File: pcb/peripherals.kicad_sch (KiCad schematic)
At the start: 35 parts, among them J2 Conn_01x24_MountingPin, J3 Conn_02x04_Odd_Even, J4 Conn_02x05_Odd_Even, SW1 SS-3235S-L1, U4 TLV74328PDBVR, U5 NRF24L01_Breakout, U6 TLV74315PDBVR, U7 BMI270, U8 HYCW110-TF10-180B, X1 OT322524MJBA4SL

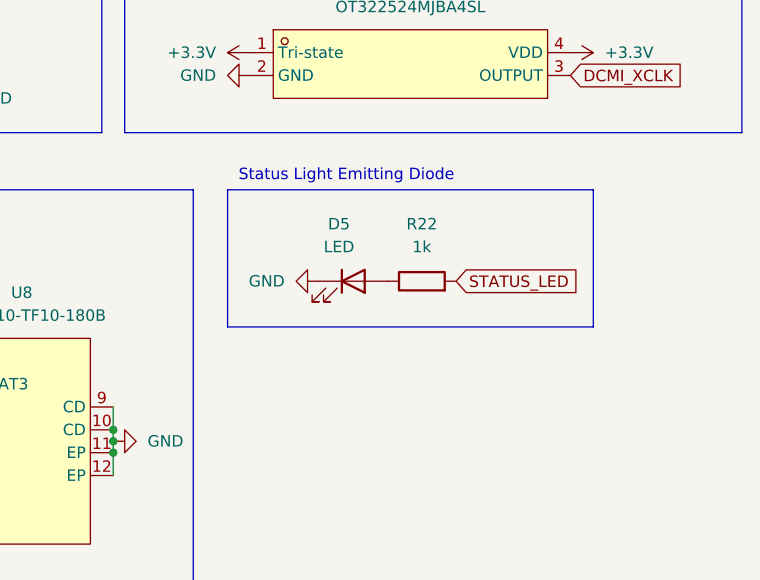
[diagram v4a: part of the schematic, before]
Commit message: [pcb] small fixes and improvements
- add two status LEDs
- move silkscreen labels for better visibility
- add more silkcreen logos/credits
- fix nrf footprint, add rf keepout zone
- add mounting holes
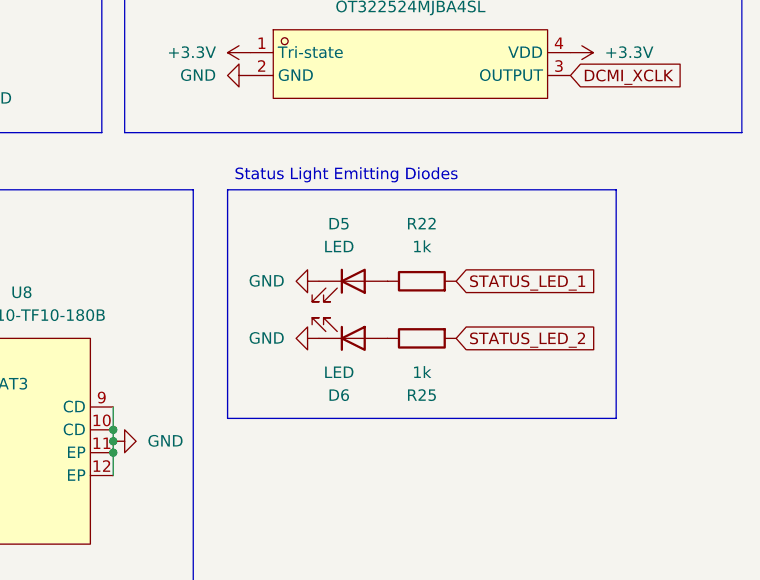
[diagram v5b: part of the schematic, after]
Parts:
- added D6: LED, LED_SMD:LED_0805_2012Metric, symbol Device:LED
- added R25: 1k, Resistor_SMD:R_0805_2012Metric, symbol Device:R
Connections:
- net GND: now also D6.1 (K)
- net STATUS_LED renamed STATUS_LED_1
- new net: D6.2 (A), R25.1
- new net STATUS_LED_2: R25.2
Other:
- note added: "Status Light Emitting Diodes"
- note removed: "Status Light Emitting Diode"
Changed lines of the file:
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@@
 	(rectangle
 		(start 165.1 100.33)
-		(end 205.74 115.57)
+		(end 208.28 125.73)
 		(stroke
 			(width 0)
@@
 		)
 	)
-	(text "Status Light Emitting Diode"
+	(text "Status Light Emitting Diodes"
 		(exclude_from_sim no)
 		(at 178.308 98.806 0)
@@
 		)
 	)
-	(global_label "STATUS_LED"
+	(global_label "STATUS_LED_1"
 		(shape input)
 		(at 190.5 110.49 0)
@@
 		)
 		(property "Intersheetrefs" "${INTERSHEET_REFS}"
-			(at 204.6732 110.49 0)
+			(at 206.8503 110.49 0)
 			(effects
 				(font
@@
 		)
 	)
+	(global_label "STATUS_LED_2"
+		(shape input)
+		(at 190.5 116.84 0)
+		(fields_autoplaced yes)
+		(effects
+			(font
+				(size 1.27 1.27)
+			)
+			(justify left)
+		)
+		(property "Intersheetrefs" "${INTERSHEET_REFS}"
+			(at 206.8503 116.84 0)
+			(effects
+				(font
+					(size 1.27 1.27)
+				)
+				(justify left)
+				(hide yes)
+			)
+		)
+	)
 	(global_label "DCMI_PWDN"
 		(shape input)
@@
 	)
 	(symbol
+		(lib_id "Device:R")
+		(at 186.69 116.84 90)
+		(mirror x)
+		(unit 1)
+		(exclude_from_sim no)
+		(in_bom yes)
+		(on_board yes)
+		(dnp no)
+		(fields_autoplaced yes)
+		(property "Reference" "R25"
+			(at 186.69 123.19 90)
+			(effects
+				(font
+					(size 1.27 1.27)
+				)
+			)
+		)
+		(property "Value" "1k"
+			(at 186.69 120.65 90)
+			(effects
+				(font
+					(size 1.27 1.27)
+				)
+			)
+		)
+		(property "Footprint" "Resistor_SMD:R_0805_2012Metric"
+			(at 186.69 115.062 90)
+			(effects
+				(font
+					(size 1.27 1.27)
+				)
+				(hide yes)
+			)
+		)
+		(property "Datasheet" "~"
+			(at 186.69 116.84 0)
+			(effects
+				(font
+					(size 1.27 1.27)
+				)
+				(hide yes)
+			)
+		)
+		(property "Description" "Resistor"
+			(at 186.69 116.84 0)
+			(effects
+				(font
+					(size 1.27 1.27)
+				)
+				(hide yes)
+			)
+		)
+		(pin "1"
+		)
+		(pin "2"
+		)
+		(instances
+			(project "astra"
+				(path "/c0be3de2-9de4-4447-aa6f-537ea5f31aac/5121fc52-65c9-43af-86a0-4c1ef24f194e"
+					(reference "R25")
+					(unit 1)
+				)
+			)
+		)
+	)
+	(symbol
 		(lib_id "power:+3.3V")
 		(at 97.79 52.07 270)
@@
 	(symbol
 		(lib_id "power:GND")
+		(at 175.26 116.84 270)
+		(mirror x)
+		(unit 1)
+		(exclude_from_sim no)
+		(in_bom yes)
+		(on_board yes)
+		(dnp no)
+		(fields_autoplaced yes)
+		(property "Reference" "#PWR083"
+			(at 168.91 116.84 0)
+			(effects
+				(font
+					(size 1.27 1.27)
+				)
+				(hide yes)
+			)
+		)
+		(property "Value" "GND"
+			(at 171.45 116.8401 90)
+			(effects
+				(font
+					(size 1.27 1.27)
+				)
+				(justify right)
+			)
+		)
+		(property "Footprint" ""
+			(at 175.26 116.84 0)
+			(effects
+				(font
+					(size 1.27 1.27)
+				)
+				(hide yes)
+			)
+		)
+		(property "Datasheet" ""
+			(at 175.26 116.84 0)
+			(effects
+				(font
+					(size 1.27 1.27)
+				)
+				(hide yes)
+			)
+		)
+		(property "Description" "Power symbol creates a global label with name \"GND\" , ground"
+			(at 175.26 116.84 0)
+			(effects
+				(font
+					(size 1.27 1.27)
+				)
+				(hide yes)
+			)
+		)
+		(pin "1"
+		)
+		(instances
+			(project "astra"
+				(path "/c0be3de2-9de4-4447-aa6f-537ea5f31aac/5121fc52-65c9-43af-86a0-4c1ef24f194e"
+					(reference "#PWR083")
+					(unit 1)
+				)
+			)
+		)
+	)
+	(symbol
+		(lib_id "power:GND")
 		(at 193.04 36.83 0)
 		(unit 1)
@@
 					(unit 1)
 				)
+			)
+		)
+	)
+	(symbol
+		(lib_id "Device:LED")
+		(at 179.07 116.84 0)
+		(mirror x)
+		(unit 1)
+		(exclude_from_sim no)
+		(in_bom yes)
+		(on_board yes)
+		(dnp no)
+		(fields_autoplaced yes)
+		(property "Reference" "D6"
+			(at 177.4825 123.19 0)
+			(effects
+				(font
+					(size 1.27 1.27)
+				)
+			)
+		)
+		(property "Value" "LED"
+			(at 177.4825 120.65 0)
+			(effects
+				(font
+					(size 1.27 1.27)
+				)
+			)
+		)
+		(property "Footprint" "LED_SMD:LED_0805_2012Metric"
+			(at 179.07 116.84 0)
+			(effects
+				(font
+					(size 1.27 1.27)
+				)
+				(hide yes)
+			)
+		)
+		(property "Datasheet" "~"
+			(at 179.07 116.84 0)
+			(effects
+				(font
+					(size 1.27 1.27)
+				)
+				(hide yes)
+			)
+		)
+		(property "Description" "Light emitting diode"
+			(at 179.07 116.84 0)
+			(effects
+				(font
+					(size 1.27 1.27)
+				)
+				(hide yes)
+			)
+		)
+		(property "Sim.Pins" "1=K 2=A"
+			(at 179.07 116.84 0)
+			(effects
+				(font
+					(size 1.27 1.27)
+				)
+				(hide yes)
+			)
+		)
+		(pin "2"
+		)
+		(pin "1"
+		)
+		(instances
+			(project "astra"
+				(path "/c0be3de2-9de4-4447-aa6f-537ea5f31aac/5121fc52-65c9-43af-86a0-4c1ef24f194e"
+					(reference "D6")
+					(unit 1)
+				)

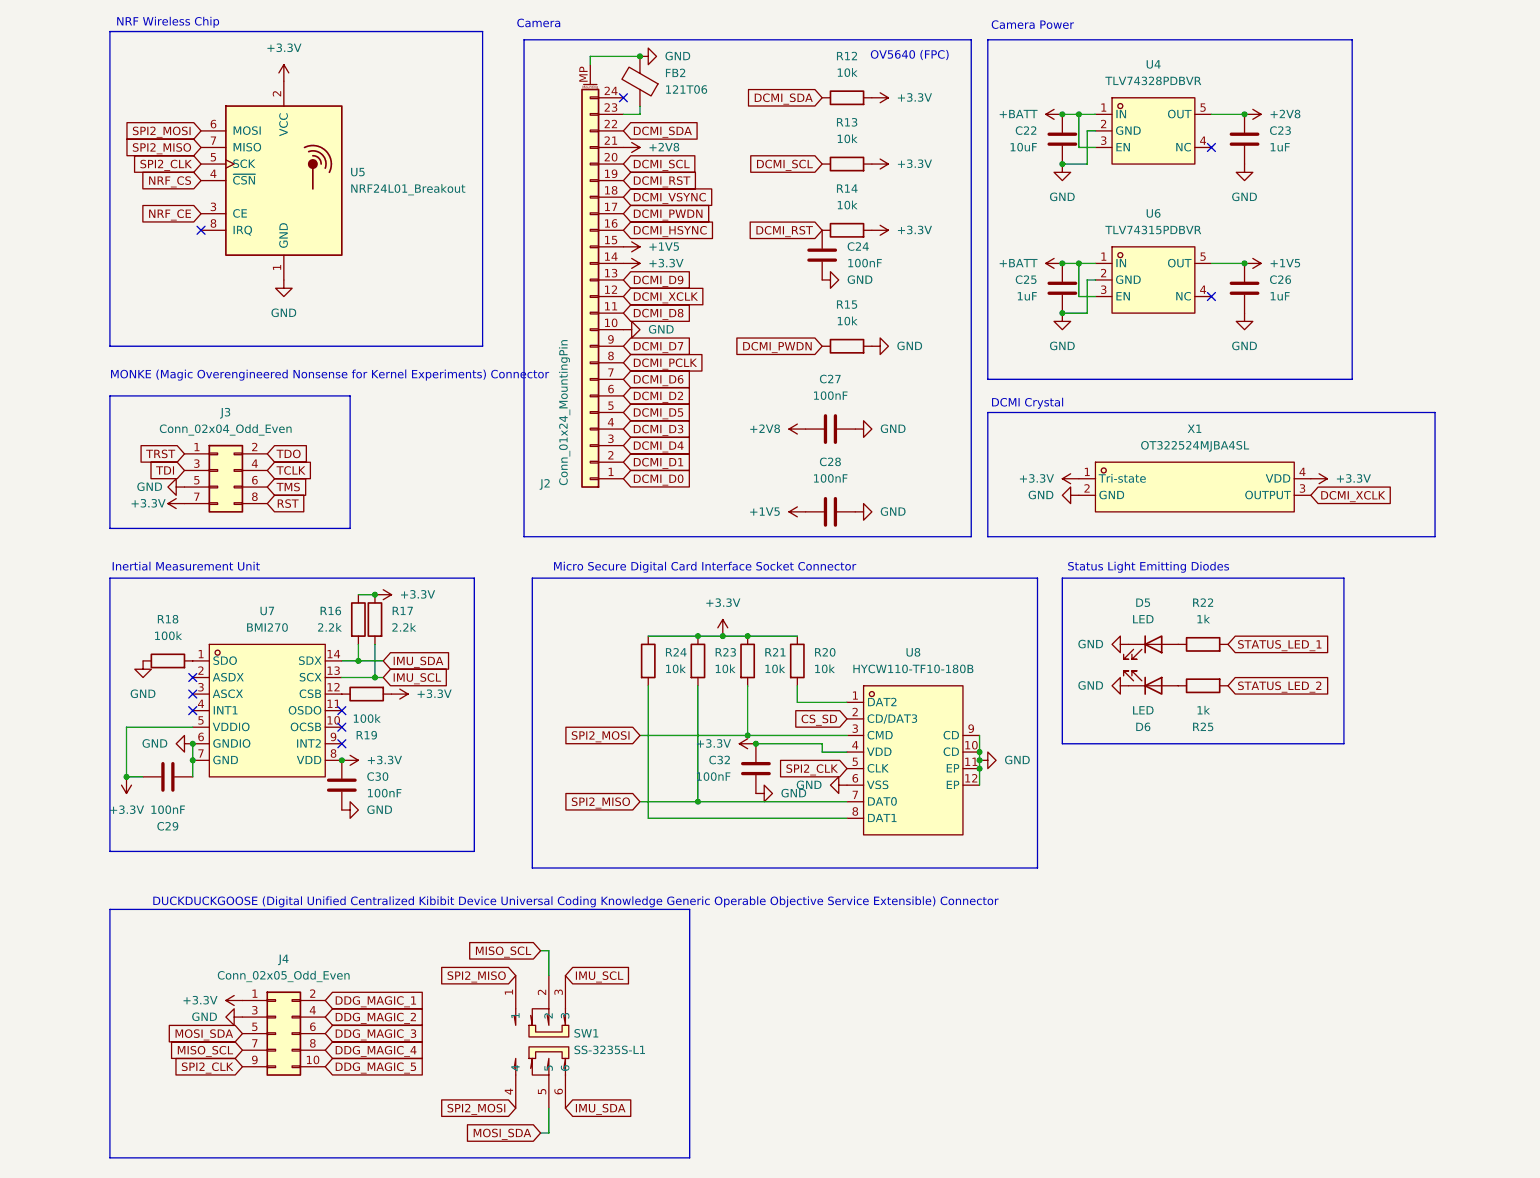
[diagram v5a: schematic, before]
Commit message: [pcb] remove on-board camera
- remove camera and all supporting components (we'll be using an external dedicated board)
- extend DDG header
- make PCB smaller
- add more silkscreen labels
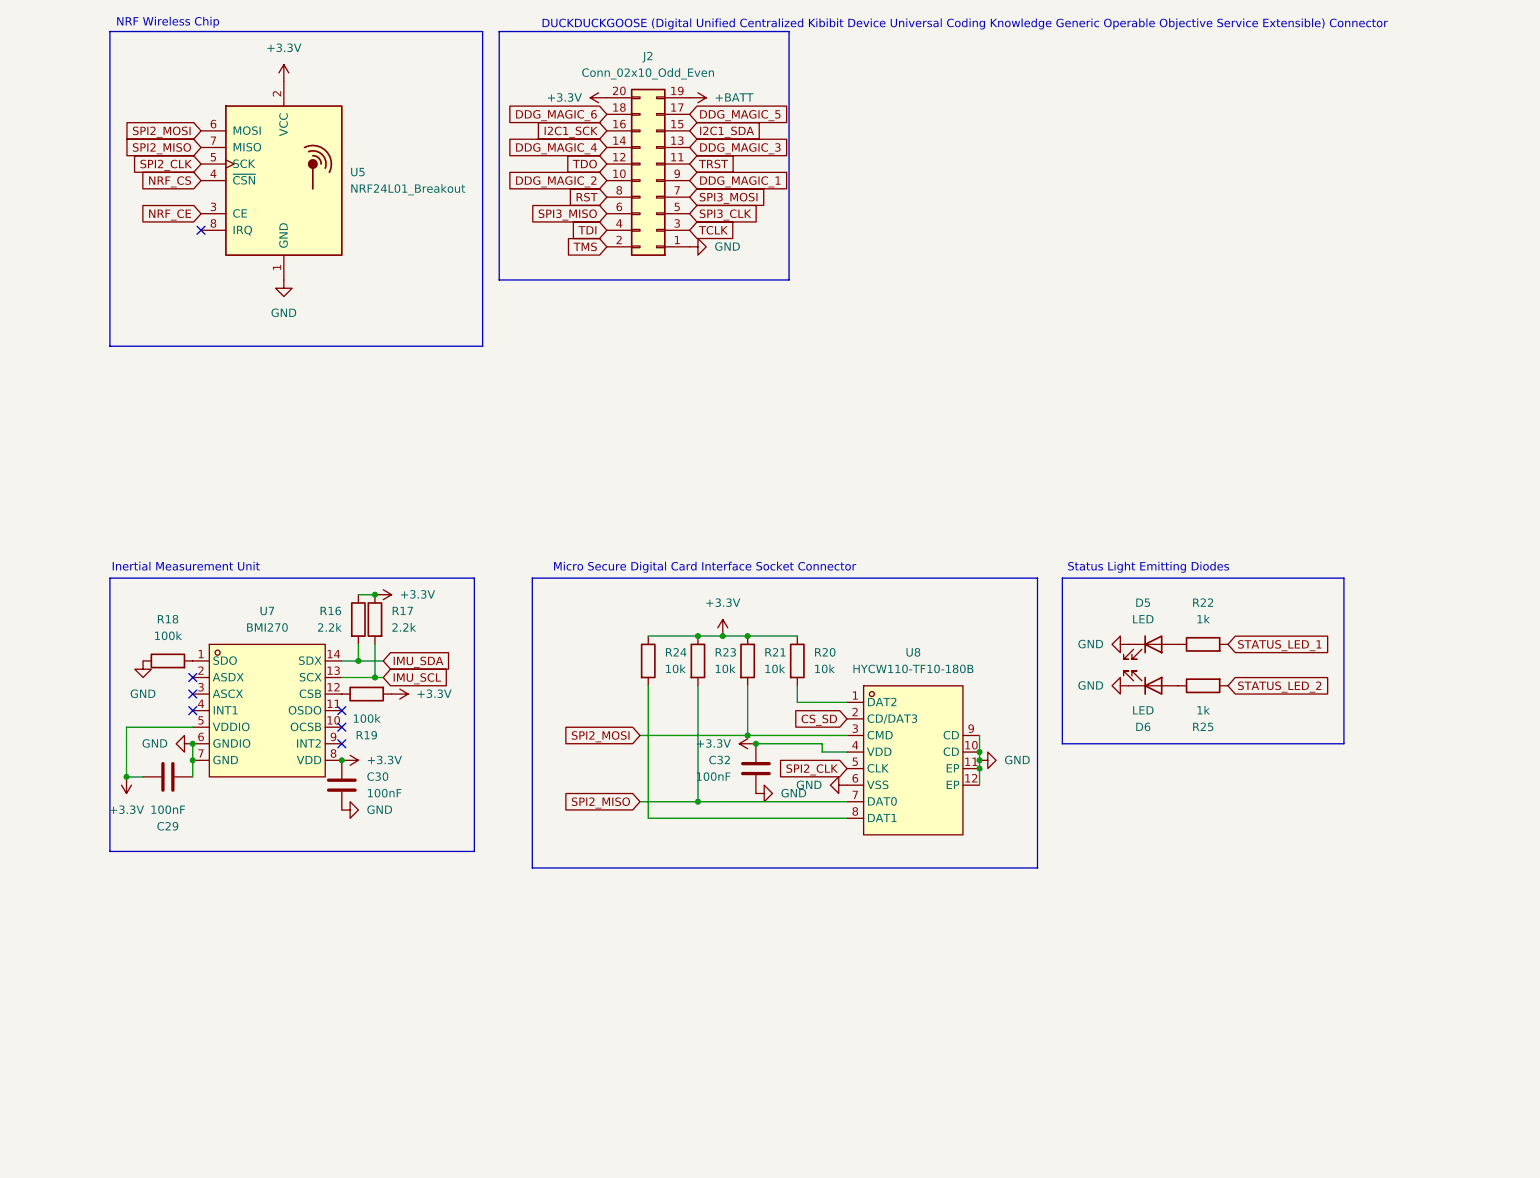
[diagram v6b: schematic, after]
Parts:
- removed C22: 10uF, Capacitor_SMD:C_0805_2012Metric_Pad1.18x1.45mm_HandSolder, symbol Device:C
- removed C23, C25, C26: 1uF, Capacitor_SMD:C_0805_2012Metric_Pad1.18x1.45mm_HandSolder, symbol Device:C
- removed C24, C27, C28: 100nF, Capacitor_SMD:C_0805_2012Metric_Pad1.18x1.45mm_HandSolder, symbol Device:C
- removed FB2: 121T06, Inductor_SMD:L_0603_1608Metric_Pad1.05x0.95mm_HandSolder, symbol Device:FerriteBead
- removed J2: Conn_01x24_MountingPin, Connector_FFC-FPC:JUSHUO_AFA07-S24FCA-00_1x24-1MP_P1.0mm_Horizontal, symbol Connector_Generic_MountingPin:Conn_01x24_MountingPin
- removed J3: Conn_02x04_Odd_Even, Connector_PinHeader_2.54mm:PinHeader_2x04_P2.54mm_Vertical, symbol Connector_Generic:Conn_02x04_Odd_Even
- removed J4: Conn_02x05_Odd_Even, Connector_PinHeader_2.54mm:PinHeader_2x05_P2.54mm_Vertical, symbol Connector_Generic:Conn_02x05_Odd_Even
- removed R12, R13, R14, R15: 10k, Resistor_SMD:R_0805_2012Metric_Pad1.20x1.40mm_HandSolder, symbol Device:R
- removed SW1: SS-3235S-L1, lcsc:SW-SMD_SS-3235S-LX, symbol lcsc:SS-3235S-L1
- removed U4: TLV74328PDBVR, Package_TO_SOT_SMD:SOT-23-5_HandSoldering, symbol lcsc:TLV74328PDBVR
- removed U6: TLV74315PDBVR, Package_TO_SOT_SMD:SOT-23-5_HandSoldering, symbol lcsc:TLV74328PDBVR
- removed X1: OT322524MJBA4SL, Crystal:Crystal_SMD_3225-4Pin_3.2x2.5mm_HandSoldering, symbol lcsc:OT322524MJBA4SL
- added J2: Conn_02x10_Odd_Even, Connector_PinHeader_2.54mm:PinHeader_2x10_P2.54mm_Vertical, symbol Connector_Generic:Conn_02x10_Odd_Even
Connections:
- net +3.3V: now also J2.20 (Pin_20)
- net +BATT: now also J2.19 (Pin_19)
- net DDG_MAGIC_1: now also J2.9 (Pin_9)
- net DDG_MAGIC_2: now also J2.10 (Pin_10)
- net DDG_MAGIC_3: now also J2.13 (Pin_13)
- net DDG_MAGIC_4: now also J2.14 (Pin_14)
- net DDG_MAGIC_5: now also J2.17 (Pin_17)
- net GND: now also J2.1 (Pin_1)
- net RST: now also J2.8 (Pin_8)
- net TCLK: now also J2.3 (Pin_3)
- net TDI: now also J2.4 (Pin_4)
- net TDO: now also J2.12 (Pin_12)
- net TMS: now also J2.2 (Pin_2)
- net TRST: now also J2.11 (Pin_11)
- new net DDG_MAGIC_6: J2.18 (Pin_18)
- new net I2C1_SCK: J2.16 (Pin_16)
- new net I2C1_SDA: J2.15 (Pin_15)
- new net SPI3_CLK: J2.5 (Pin_5)
- new net SPI3_MISO: J2.6 (Pin_6)
- new net SPI3_MOSI: J2.7 (Pin_7)
- no-connect marks 10 -> 7
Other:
- note removed: "Camera"
- note removed: "Camera Power"
- note removed: "DCMI Crystal"
- note removed: "MONKE (Magic Overengineered Nonsense for Kernel Experiments) Connector"
- note removed: "OV5640 (FPC)"
